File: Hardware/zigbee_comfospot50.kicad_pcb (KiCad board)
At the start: 4 copper layers, 62 x 26.5 mm, 19 parts, among them J1 690357101472, J2 690367191472, J3 Conn_01x04, SW1 SW_Push, SW2 SW_Push, U1 ESP32-H2-WROOM-02C

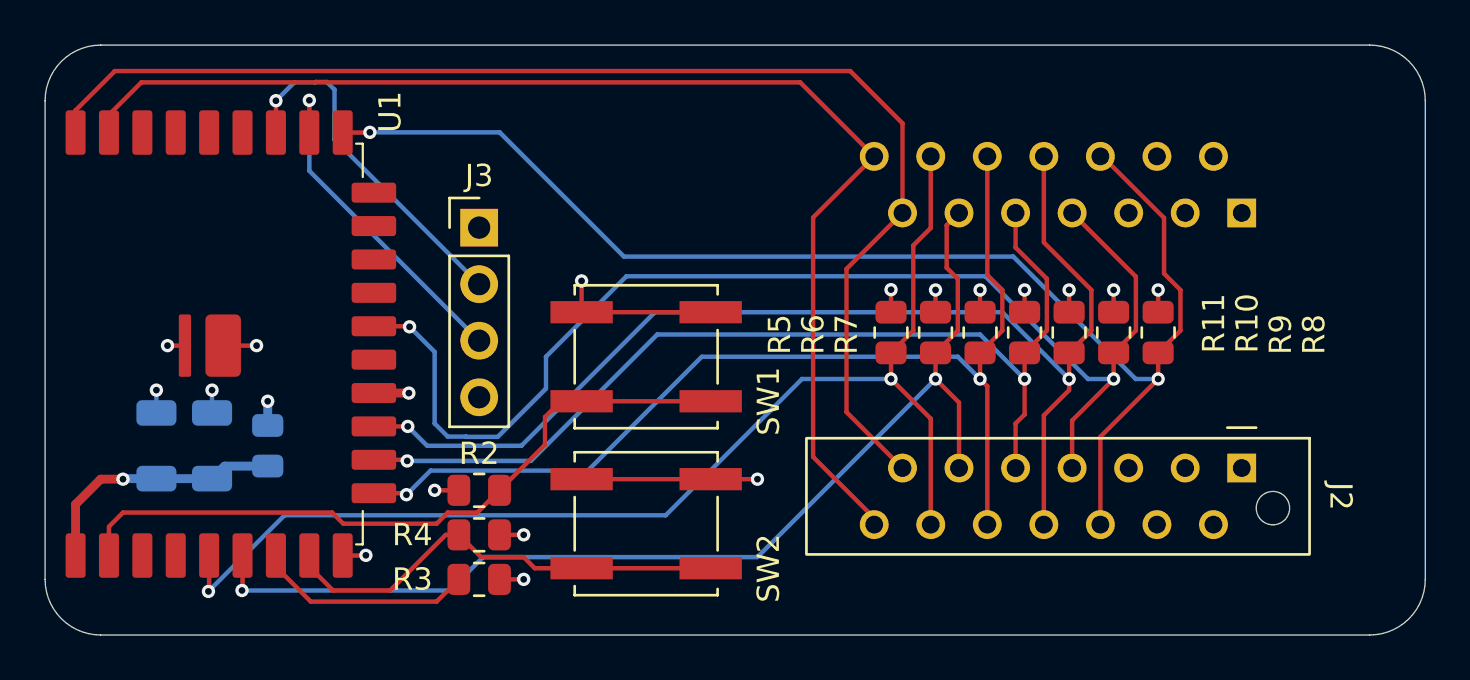
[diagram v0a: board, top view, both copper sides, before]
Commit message: Shortened PCB to fit Comfospot 50 available space. NOT YET TESTED in HW.
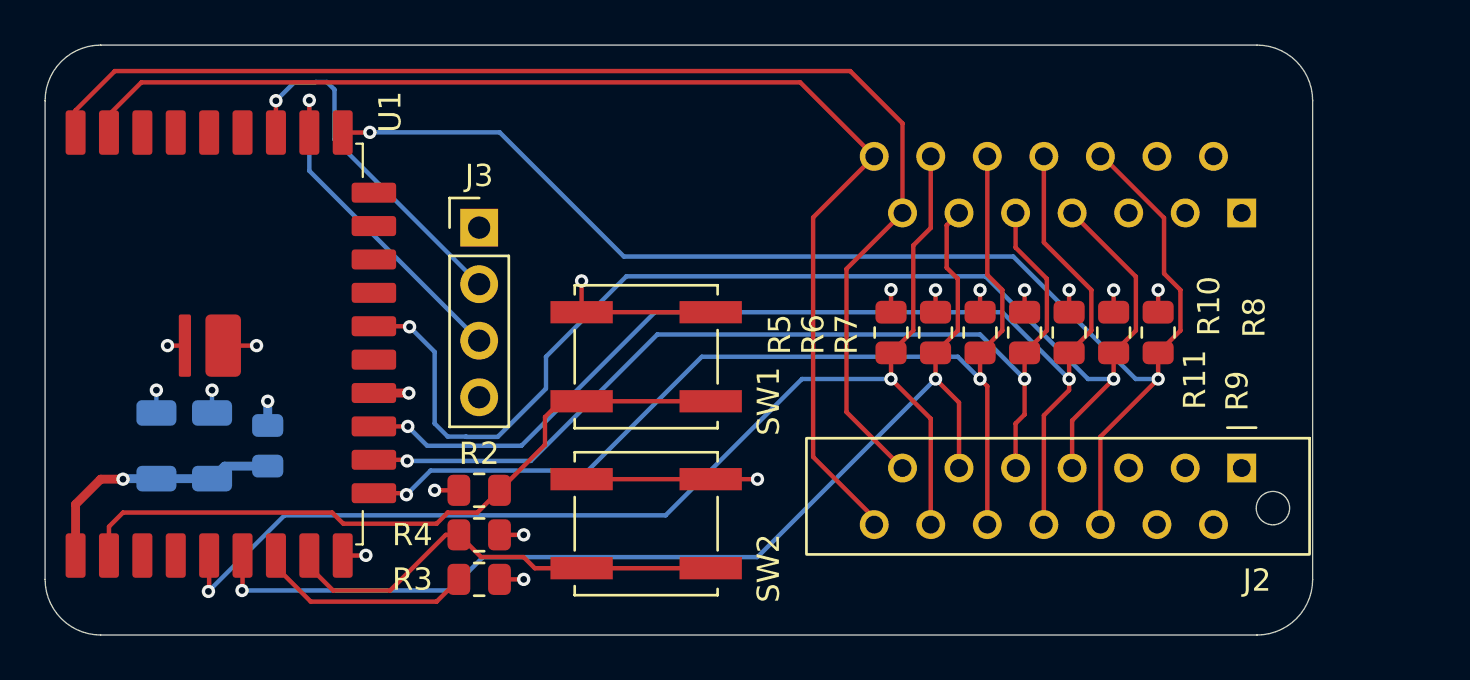
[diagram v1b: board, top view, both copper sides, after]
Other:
- board size 62 x 26.5 mm -> 56.9 x 26.5 mm
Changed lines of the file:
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@@
 			(psa4output no)
 			(plot_black_and_white yes)
-			(plotinvisibletext no)
 			(sketchpadsonfab no)
 			(plotpadnumbers no)
@@
 		(tags "resistor")
 		(property "Reference" "R8"
-			(at 0.0875 -7 90)
+			(at -0.6775 -4.313 90)
 			(layer "F.SilkS")
 			(effects
@@
 		(tags "THT")
 		(property "Reference" "J2"
-			(at 1.27 -4.445 270)
+			(at 5.046 -0.685 0)
 			(unlocked yes)
 			(layer "F.SilkS")
@@
 		(tags "resistor")
 		(property "Reference" "R11"
-			(at -0.4125 -8.5 90)
+			(at 2.1165 -7.646 90)
 			(layer "F.SilkS")
 			(effects
@@
 		(tags "resistor")
 		(property "Reference" "R9"
-			(at 0.0875 -7.5 90)
+			(at 2.6245 -5.551 90)
 			(layer "F.SilkS")
 			(effects
@@
 		(tags "resistor")
 		(property "Reference" "R10"
-			(at -0.4125 -8 90)
+			(at -1.1855 -6.281 90)
 			(layer "F.SilkS")
 			(effects
@@
 		(tags "THT")
 		(property "Reference" "J1"
-			(at 1.27 3.175 270)
+			(at 5.04 0.685 0)
 			(unlocked yes)
 			(layer "B.SilkS")
@@
 	)
 	(gr_arc
-		(start 160 90)
-		(mid 161.767767 90.732233)
-		(end 162.5 92.5)
+		(start 154.94 90)
+		(mid 156.707767 90.732233)
+		(end 157.44 92.5)
 		(stroke
 			(width 0.05)
@@
 	)
 	(gr_arc
-		(start 162.5 114)
-		(mid 161.767767 115.767767)
-		(end 160 116.5)
+		(start 157.44 114)
+		(mid 156.707767 115.767767)
+		(end 154.94 116.5)
 		(stroke
 			(width 0.05)
@@
 	)
 	(gr_line
-		(start 162.5 114)
-		(end 162.5 92.5)
+		(start 157.44 114)
+		(end 157.44 92.5)
 		(stroke
 			(width 0.05)
@@
 	(gr_line
 		(start 103 116.5)
-		(end 160 116.5)
+		(end 154.94 116.5)
 		(stroke
 			(width 0.05)
@@
 	(gr_line
 		(start 103 90)
-		(end 160 90)
+		(end 154.94 90)
 		(stroke
 			(width 0.05)
@@
 		(polygon
 			(pts
-				(xy 100.5 90) (xy 162.5 90) (xy 162.5 116.5) (xy 100.5 116.5)
+				(xy 100.5 90) (xy 157.42 90) (xy 157.42 116.5) (xy 100.5 116.5)
 			)
 		)
@@
 		(polygon
 			(pts
-				(xy 100.5 90) (xy 162.5 90) (xy 162.5 116.5) (xy 100.5 116.5)
+				(xy 100.5 90) (xy 157.42 90) (xy 157.42 116.5) (xy 100.5 116.5)
 			)
 		)
